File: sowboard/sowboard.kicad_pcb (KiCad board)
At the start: 2 copper layers, 38 x 42 mm, 38 parts, among them J1 Conn_01x10_MountingPin, J2 Conn_01x10_MountingPin, J3 Conn_01x10_MountingPin, J4 Conn_01x10_MountingPin, U1 ProMicro, U2 PJ-320A, U3 PJ-320A

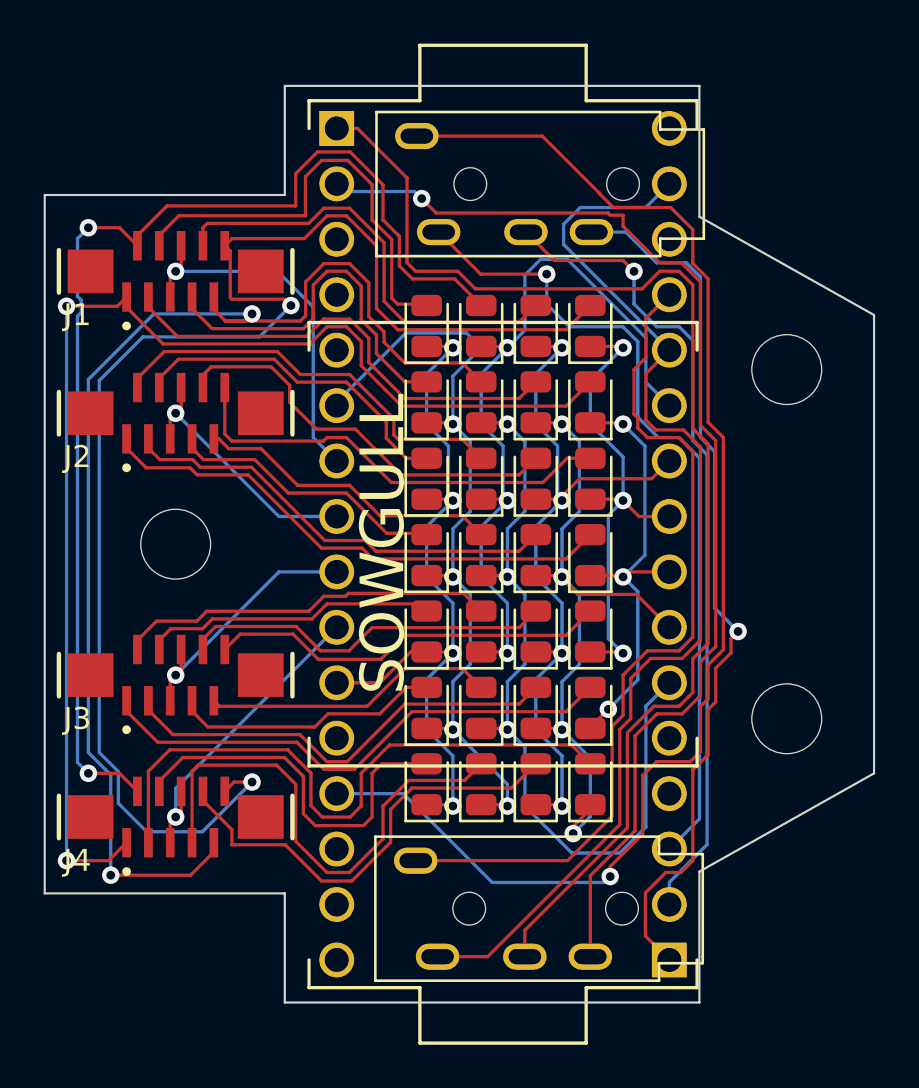
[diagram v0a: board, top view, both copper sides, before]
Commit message: Increase clearance for audio plug
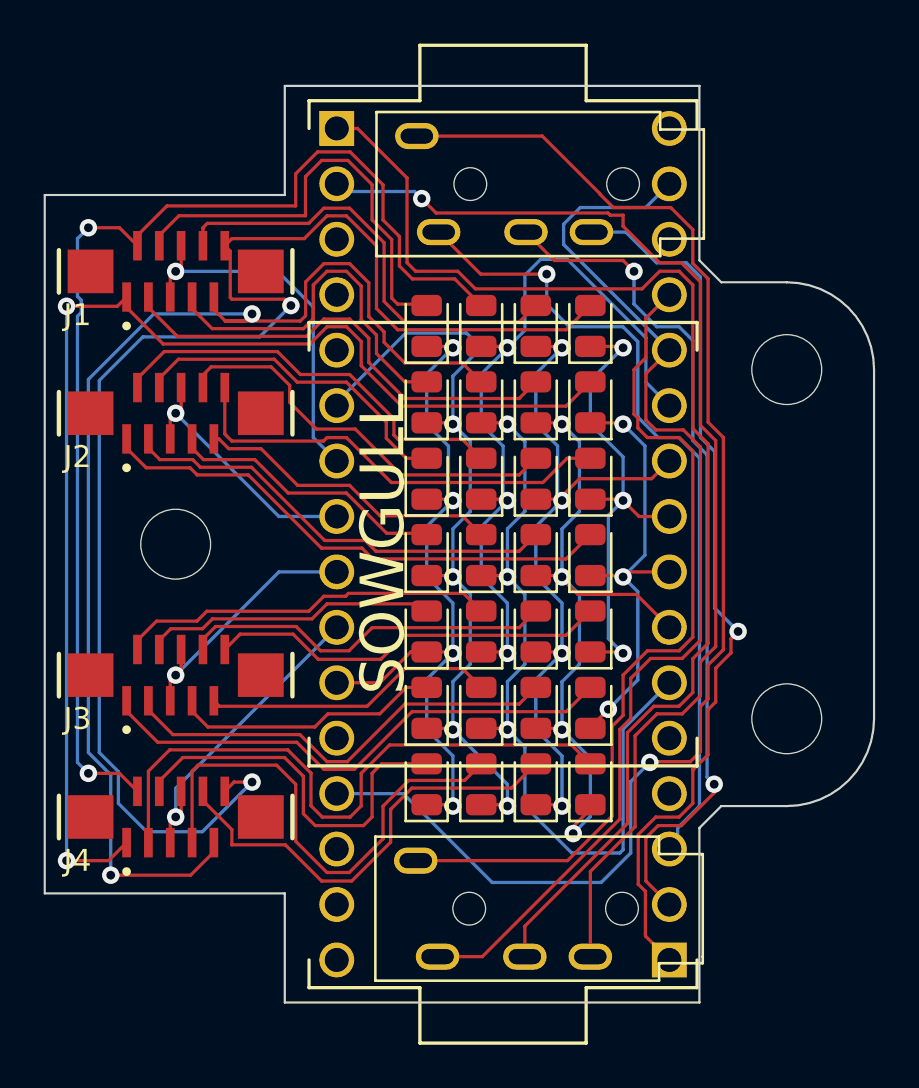
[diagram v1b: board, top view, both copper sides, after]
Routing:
- net Net-(U2-Ring1): track 37.4 -> 39.2 mm, vias 1 -> 2
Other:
- outline, holes or cut-outs redrawn

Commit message: Improve sowboard layout a bit, switch the data pin to PD2, and work around DRC warnings
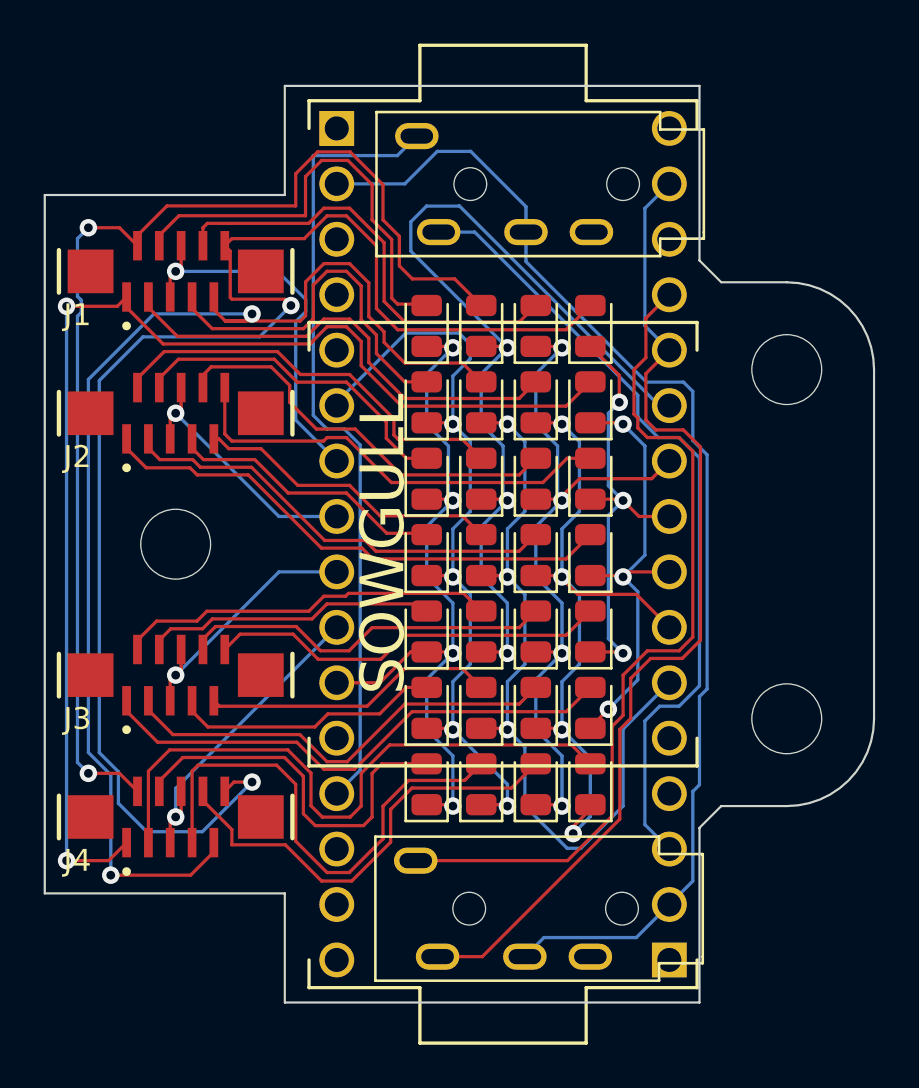
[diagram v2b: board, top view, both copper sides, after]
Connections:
- J1 pad S1: (no net) -> unconnected-(J1-PadS1)
- J1 pad S2: (no net) -> unconnected-(J1-PadS2)
- J2 pad S1: (no net) -> unconnected-(J2-PadS1)
- J2 pad S2: (no net) -> unconnected-(J2-PadS2)
- J3 pad S1: (no net) -> unconnected-(J3-PadS1)
- J3 pad S2: (no net) -> unconnected-(J3-PadS2)
- J4 pad S1: (no net) -> unconnected-(J4-PadS1)
- J4 pad S2: (no net) -> unconnected-(J4-PadS2)
- U1 pad 1: Net-(U3-Ring1) -> unconnected-(U1-TX-Pad1)
- U1 pad 1B: Net-(U2-Ring2) -> unconnected-(U1-TX-Pad1B)
- U1 pad 2: Net-(U3-Ring2) -> Net-(U2-Ring1)
- U2 pad 4: Net-(U2-Ring2) -> unconnected-(U2-Ring2-Pad4)
- U3 pad 3: Net-(U3-Ring1) -> Net-(U2-Ring1)
- U3 pad 4: Net-(U3-Ring2) -> unconnected-(U3-Ring2-Pad4)
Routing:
- net Net-(U3-Ring1): track 57.4 -> 0.00 mm
- net Net-(U3-Ring2): track 52.9 -> 0.00 mm, vias 1 -> 0
- net Net-(U2-Ring2): track 41.0 -> 0.00 mm, vias 1 -> 0
- net Net-(U2-Sleeve): track 62.1 -> 36.1 mm, vias 1 -> 0
- net Net-(U2-Ring1): track 39.2 -> 55.1 mm, vias 2 -> 0
- net ROW_2: track 34.1 -> 43.1 mm
- net Net-(U1-F4): track 50.4 -> 45.6 mm
- net ROW_8: track 22.7 -> 21.0 mm
- net ROW_7: track 36.8 -> 35.5 mm
- net Net-(U2-Tip): track 37.6 -> 36.8 mm, vias 1 -> 0
- net ROW_5: track 36.7 -> 36.0 mm
